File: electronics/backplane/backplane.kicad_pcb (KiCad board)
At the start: 2 copper layers, 46 x 100 mm, 22 parts, among them J1 USB_C_SOCKET_RA_PTH_SIMPLE, P1 JST_SH_4_RA, P2 JST_SH_4_RA, P3 JST_SH_4_RA, P4 JST_SH_4_RA, P5 PAD_SOLDER_2mm, SW1 B3U-1000P_SPST-NO_SMD, SW2 B3U-1000P_SPST-NO_SMD, U1 USBLC6, X1 MICROMOD_PROCESSOR_SOCKET, X2 SWD_SMT_SOCKET, X3 MICROMOD_FUNCTION_BOARD_SOCKET

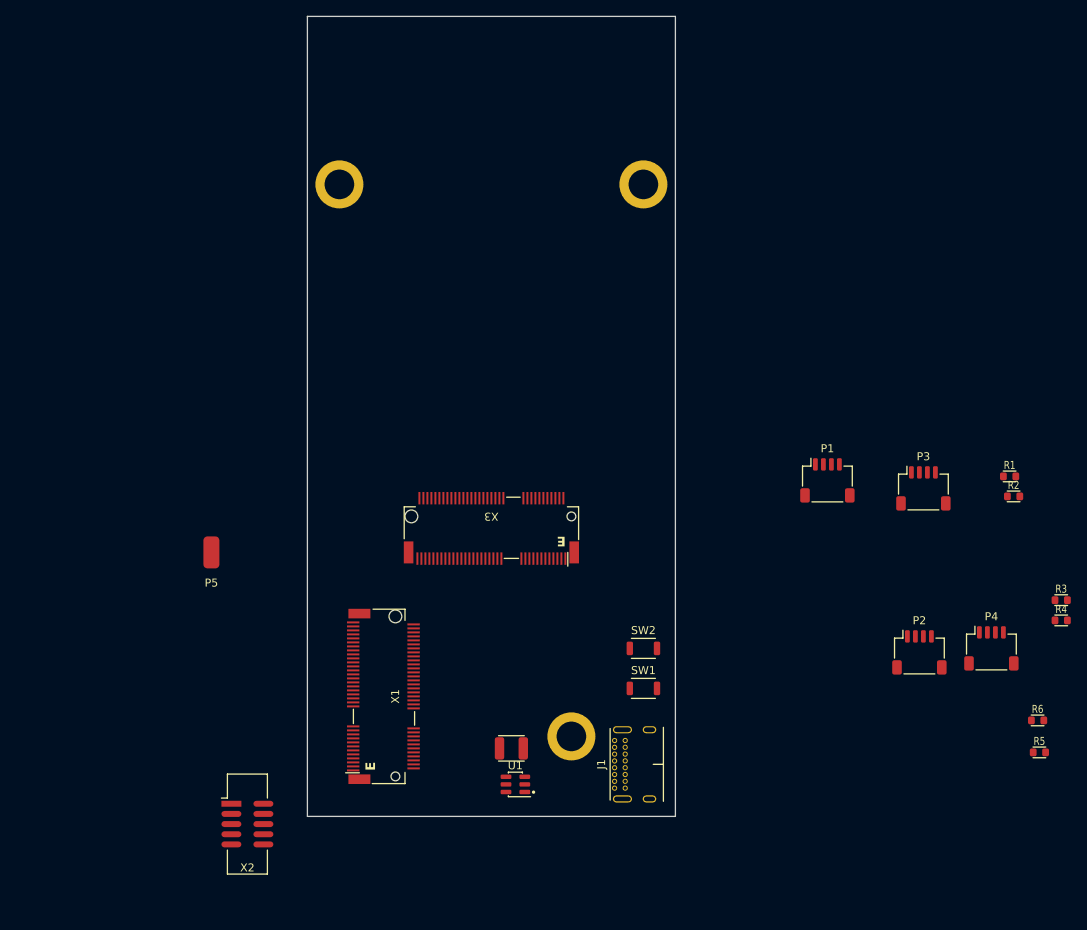
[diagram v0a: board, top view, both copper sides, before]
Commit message: Backplane schematic capture and PCB shape
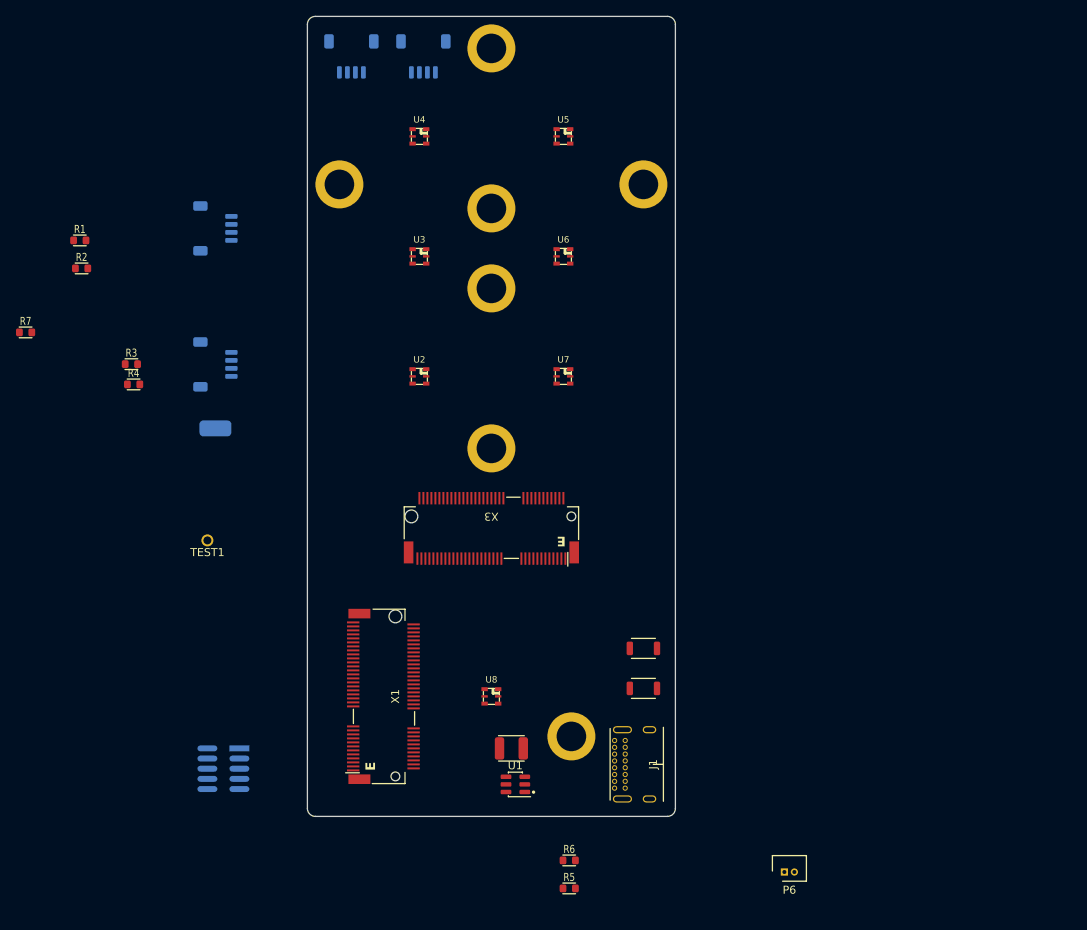
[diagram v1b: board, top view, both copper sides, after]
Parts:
- added MNT4: M2.5_SMD_4.0MM_THREADED, Applidyne_Mount:9774040151R, B.Cu at (123.0, 104.0)
- added MNT5: M2.5_SMD_4.0MM_THREADED, Applidyne_Mount:9774040151R, B.Cu at (123.0, 74.0)
- added MNT6: M2.5_SMD_4.0MM_THREADED, Applidyne_Mount:9774040151R, B.Cu at (123.0, 84.0)
- added MNT7: M2.5_SMD_4.0MM_THREADED, Applidyne_Mount:9774040151R, B.Cu at (123.0, 54.0)
- added P6: MOLEX_PICO_PTH_VERT_2_WAY, Applidyne_Connector_Molex:MOLEX_PICOBLADE_53047-0210, F.Cu at (159.6, 156.9)
- added R7: 10K0_1608M, Applidyne_Resistor:RESC1608X50N, F.Cu at (64.8, 89.5)
- added TEST1: CLIP_HOOK_PURPLE, Applidyne_Test:KEYSTONE_5119, F.Cu at (87.5, 115.5)
- added U2: APA102-2020, Applidyne_LED:AP102_200X200X90L, F.Cu at (114.0, 95.0)
- added U3: APA102-2020, Applidyne_LED:AP102_200X200X90L, F.Cu at (114.0, 80.0)
- added U4: APA102-2020, Applidyne_LED:AP102_200X200X90L, F.Cu at (114.0, 65.0)
- added U5: APA102-2020, Applidyne_LED:AP102_200X200X90L, F.Cu at (132.0, 65.0)
- added U6: APA102-2020, Applidyne_LED:AP102_200X200X90L, F.Cu at (132.0, 80.0)
- added U7: APA102-2020, Applidyne_LED:AP102_200X200X90L, F.Cu at (132.0, 95.0)
- added U8: APA102-2020, Applidyne_LED:AP102_200X200X90L, F.Cu at (123.0, 135.0)
- P1: value JST_SH_4_RA -> PAD_SOLDER_2mm; footprint Applidyne_Connector_JST:SM04B-SRSS-TB -> Applidyne_Connector:PAD_SOLDER_2mm; moved to B.Cu
- P2, P3, P4, X2: moved to B.Cu
- P5: value PAD_SOLDER_2mm -> JST_SH_4_RA; footprint Applidyne_Connector:PAD_SOLDER_2mm -> Applidyne_Connector_JST:SM04B-SRSS-TB; moved to B.Cu
- moved R2 119.9 mm to (71.8, 81.5)
- moved R1 119.9 mm to (71.5, 78.0)
- moved R3 119.9 mm to (78.0, 93.5)
- moved R4 119.6 mm to (78.3, 96.0)
- moved P4 103.3 mm to (88.5, 93.5), turned to 90 degrees
- moved P2 102.9 mm to (105.5, 55.0)
- moved P3 82.6 mm to (114.5, 55.0)
- moved P1 76.8 mm to (88.5, 101.5), turned to -90 degrees
- moved R5 61.2 mm to (132.7, 159.0)
- moved R6 61.1 mm to (132.7, 155.5)
- moved P5 40.5 mm to (88.5, 76.5), turned to 90 degrees
- moved X2 7.54 mm to (89.5, 144.0)
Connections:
- net /SWDCLK renamed /Processor/SWDCLK
- net /SWDIO renamed /Processor/SWDIO
- net /SWO renamed /Processor/SWO
- net /USBC_N renamed /USB Input/USBC_N
- net /USBC_P renamed /USB Input/USBC_P
- net /USB_D+ renamed /Processor/NATIVE.D+
- net /USB_D- renamed /Processor/NATIVE.D-
- net /USB_VCC renamed /Processor/USB_VCC
- net /~{BOOT} renamed /Processor/~{BOOT}
- net /~{RESET} renamed /Processor/~{RESET}
- MNT2 pad 1: unconnected-(MNT2-Pad1) -> GND
- MNT3 pad 1: unconnected-(MNT3-Pad1) -> GND
- P1 pad 1: GND -> /Expansion IO/~{I2C_INT}
- P2 pad 3: /I2C_SDA1 -> /Expansion IO/I2C_SDA0
- P2 pad 4: /I2C_SCL1 -> /Expansion IO/I2C_SCL0
- P3 pad 3: /I2C_SDA0 -> /Expansion IO/I2C_SDA1
- P3 pad 4: /I2C_SCL0 -> /Expansion IO/I2C_SCL1
- P4 pad 3: /I2C_SDA1 -> /Expansion IO/I2C_SDA0
- P4 pad 4: /I2C_SCL1 -> /Expansion IO/I2C_SCL0
- P5 pad 1: /~{I2C_INT} -> GND
- R1 pad 2: /I2C_SDA0 -> /Function Board/SDA
- R2 pad 2: /I2C_SCL0 -> /Function Board/SCL
- R3 pad 2: /I2C_SDA1 -> /Processor/I2C1.SDA
- R4 pad 2: /I2C_SCL1 -> /Processor/I2C1.SCL
- R5 pad 1: Net-(J1-CC2) -> Net-(J1-CC1)
- R6 pad 1: Net-(J1-CC1) -> Net-(J1-CC2)
- X1 pad 10: unconnected-(X1-D0-Pad10) -> /Function Board/FN_~{INT}
- X1 pad 12: /I2C_SDA0 -> /Function Board/SDA
- X1 pad 13: unconnected-(X1-UART_RTS1-Pad13) -> /Function Board/RTS
- X1 pad 14: /I2C_SCL0 -> /Function Board/SCL
- X1 pad 15: unconnected-(X1-UARTCTS1-Pad15) -> /Function Board/CTS
- X1 pad 16: /~{I2C_INT} -> /Function Board/~{FN_I2C_INT}
- X1 pad 17: unconnected-(X1-UART_TX1-Pad17) -> /Function Board/TX
- X1 pad 19: unconnected-(X1-UART_RX1-Pad19) -> /Function Board/RX
- X1 pad 2: unconnected-(X1-3V3-Pad2) -> +3.3V
- X1 pad 20: unconnected-(X1-UART_RX2-Pad20) -> /Processor/UART1.RX
- X1 pad 22: unconnected-(X1-UART_TX2-Pad22) -> /Processor/UART1.TX
- X1 pad 32: unconnected-(X1-PWM0-Pad32) -> /Function Board/FN_PWM
- X1 pad 34: unconnected-(X1-A0-Pad34) -> /Function Board/FN_ANALOG
- X1 pad 35: unconnected-(X1-USBHOST_D+-Pad35) -> /Function Board/D+
- X1 pad 37: unconnected-(X1-USBHOST_D--Pad37) -> /Function Board/D-
- X1 pad 4: unconnected-(X1-3V3_EN-Pad4) -> /Processor/3V3_PWR_EN
- X1 pad 40: unconnected-(X1-G0/BUS0-Pad40) -> /Function Board/G0
- X1 pad 41: unconnected-(X1-CAN_RX-Pad41) -> /Function Board/CAN.RX
- X1 pad 42: unconnected-(X1-G1/BUS1-Pad42) -> /Function Board/G1
- X1 pad 43: unconnected-(X1-CAN_TX-Pad43) -> /Function Board/CAN.TX
- X1 pad 44: unconnected-(X1-G2/BUS2-Pad44) -> /Function Board/G2
- X1 pad 46: unconnected-(X1-G3/BUS3-Pad46) -> /Function Board/G3
- X1 pad 48: unconnected-(X1-G4/BUS4-Pad48) -> /Function Board/G4
- X1 pad 51: /I2C_SDA1 -> /Processor/I2C1.SDA
- X1 pad 53: /I2C_SCL1 -> /Processor/I2C1.SCL
- X1 pad 55: unconnected-(X1-~{SPI_CS}-Pad55) -> /Function Board/~{CS}
- X1 pad 57: unconnected-(X1-SPI_SCK-Pad57) -> /Function Board/CLK
- X1 pad 59: unconnected-(X1-SPI_COPI-Pad59) -> /Function Board/COPI
- X1 pad 60: unconnected-(X1-SPI_SCK1/SDIO_CLK-Pad60) -> /Processor/SPI1.CLK
- X1 pad 61: unconnected-(X1-SPI_CIPO-Pad61) -> /Function Board/CIPO
- X1 pad 62: unconnected-(X1-SPI_COPI1/SDIO_CMD-Pad62) -> /Processor/SPI1.COPI
- X1 pad 64: unconnected-(X1-SPI_CIPO1/SDIO_DATA0-Pad64) -> /Processor/SPI1.CIPO
- X1 pad 70: unconnected-(X1-~{SPI_CS1}/SDIO_DATA3-Pad70) -> /Processor/SPI1.~{CS}
- X1 pad 74: unconnected-(X1-3V3-Pad74) -> +3.3V
- X3 pad 1: unconnected-(X3-GND-Pad1) -> GND
- X3 pad 13: unconnected-(X3-FUNC_TX-Pad13) -> /Function Board/RX
- X3 pad 15: unconnected-(X3-FUNC_RX-Pad15) -> /Function Board/TX
- X3 pad 16: unconnected-(X3-FUNC_RTS-Pad16) -> /Function Board/CTS
- X3 pad 18: unconnected-(X3-FUNC_CTS-Pad18) -> /Function Board/RTS
- X3 pad 19: unconnected-(X3-I2C_SDA-Pad19) -> /Function Board/SDA
- X3 pad 2: unconnected-(X3-GND-Pad2) -> GND
- X3 pad 21: unconnected-(X3-I2C_SCL-Pad21) -> /Function Board/SCL
- X3 pad 23: unconnected-(X3-~{I2C_INT}-Pad23) -> /Function Board/~{FN_I2C_INT}
- X3 pad 3: unconnected-(X3-SPI_SCK-Pad3) -> /Function Board/CLK
- X3 pad 32: unconnected-(X3-EEPROM_A2-Pad32) -> GND
- X3 pad 33: unconnected-(X3-GND-Pad33) -> GND
- X3 pad 34: unconnected-(X3-EEPROM_A1-Pad34) -> GND
- X3 pad 35: unconnected-(X3-USBHOST_D+-Pad35) -> /Function Board/D+
- X3 pad 36: unconnected-(X3-EEPROM_A0-Pad36) -> GND
- X3 pad 37: unconnected-(X3-USBHOST_D--Pad37) -> /Function Board/D-
- X3 pad 38: unconnected-(X3-A0-Pad38) -> /Function Board/FN_ANALOG
- X3 pad 39: unconnected-(X3-GND-Pad39) -> GND
- X3 pad 40: unconnected-(X3-EEPROM_WP-Pad40) -> Net-(TEST1-PAD)
- X3 pad 41: unconnected-(X3-CAN_TX-Pad41) -> /Function Board/CAN.RX
- X3 pad 43: unconnected-(X3-CAN_RX-Pad43) -> /Function Board/CAN.TX
- X3 pad 45: unconnected-(X3-GND-Pad45) -> GND
- X3 pad 47: unconnected-(X3-F0/~{INT}-Pad47) -> /Function Board/FN_~{INT}
- X3 pad 49: unconnected-(X3-F1/~{CS}-Pad49) -> /Function Board/~{CS}
- X3 pad 5: unconnected-(X3-SPI_SDI-Pad5) -> /Function Board/COPI
- X3 pad 51: unconnected-(X3-F2/PWM-Pad51) -> /Function Board/FN_PWM
- X3 pad 53: unconnected-(X3-F3-Pad53) -> /Function Board/G0
- X3 pad 55: unconnected-(X3-F4-Pad55) -> /Function Board/G1
- X3 pad 57: unconnected-(X3-F5-Pad57) -> /Function Board/G2
- X3 pad 59: unconnected-(X3-F6-Pad59) -> /Function Board/G3
- X3 pad 61: unconnected-(X3-F7-Pad61) -> /Function Board/G4
- X3 pad 7: unconnected-(X3-SPI_SDO-Pad7) -> /Function Board/CIPO
- X3 pad 71: unconnected-(X3-PWR_EN-Pad71) -> /Function Board/FN_PWR_EN
- X3 pad 72: unconnected-(X3-VCC-Pad72) -> Net-(X3-VCC-Pad72)
- X3 pad 73: unconnected-(X3-3V3-Pad73) -> +3.3V
- X3 pad 74: unconnected-(X3-VCC-Pad74) -> Net-(X3-VCC-Pad72)
- X3 pad 75: unconnected-(X3-GND-Pad75) -> GND
- X3 pad 8: unconnected-(X3-GND-Pad8) -> GND
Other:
- outline, holes or cut-outs redrawn
- copper layers 2 -> 4
- board text added: "QWIIC MODULE BAY"

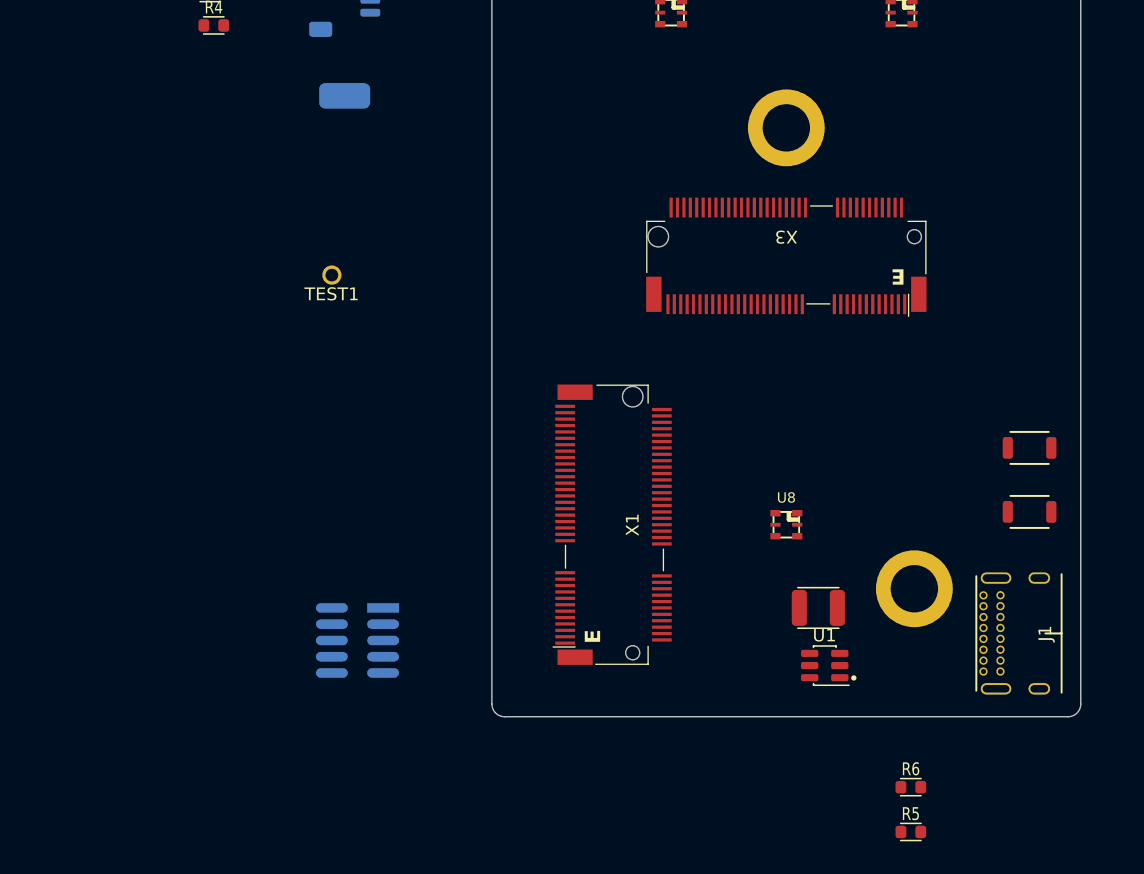
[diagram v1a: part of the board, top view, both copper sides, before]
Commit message: Continue backplane PCB
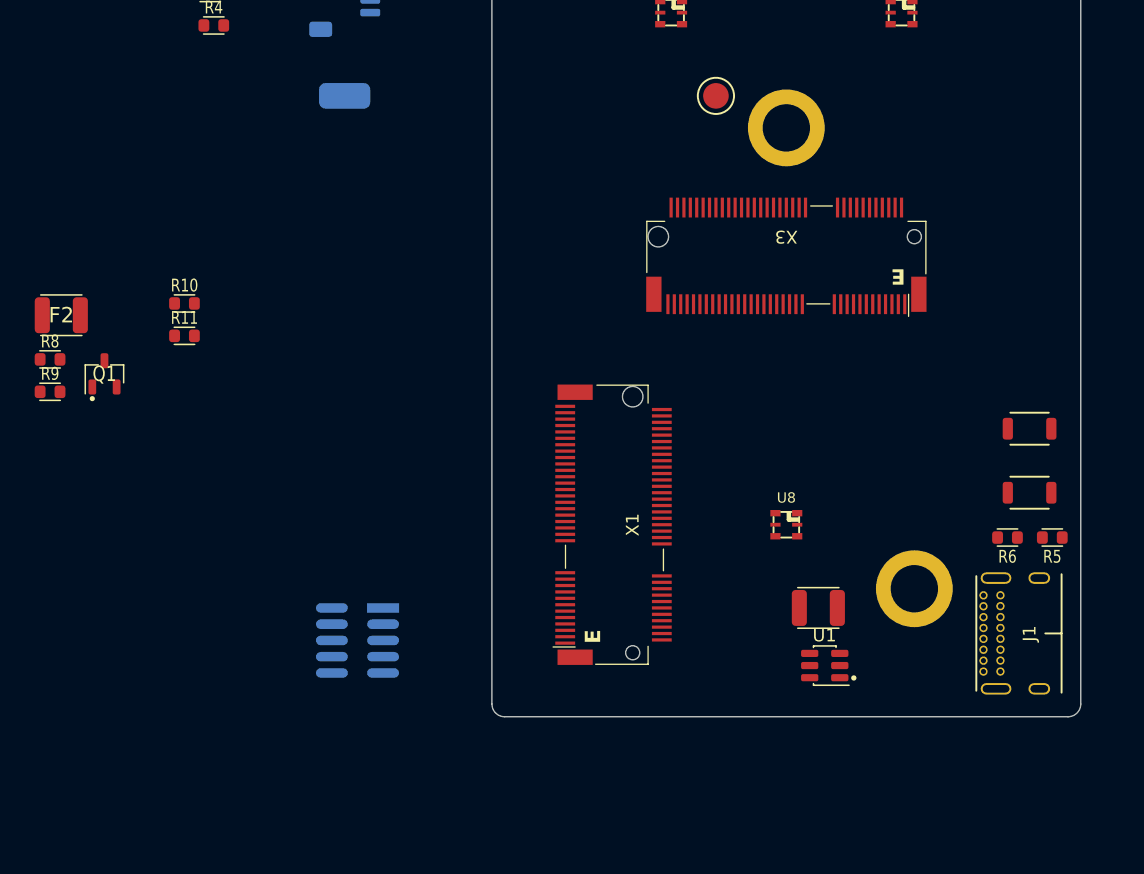
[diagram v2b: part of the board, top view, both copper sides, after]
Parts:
- removed TEST1: CLIP_HOOK_PURPLE, Applidyne_Test:KEYSTONE_5119
- added F2: 0.5A_1210L_PTC, Applidyne_Fuse:FUSC3225X85L50N, F.Cu at (66.4, 118.6)
- added Q1: 2N7002P, Applidyne_SOT:SOT95P240X110-3L16N, F.Cu at (69.7, 123.2)
- added R10: 20K0_1608M, Applidyne_Resistor:RESC1608X50N, F.Cu at (76.0, 117.7)
- added R11: 10K0_1608M, Applidyne_Resistor:RESC1608X50N, F.Cu at (76.0, 120.2)
- added R8: 10R_1608M, Applidyne_Resistor:RESC1608X50N, F.Cu at (65.5, 122.1)
- added R9: 10K0_1608M, Applidyne_Resistor:RESC1608X50N, F.Cu at (65.5, 124.6)
- added TEST2: PROBE_PAD, Applidyne_Test:TP200, F.Cu at (117.5, 101.5)
- moved R5 25.5 mm to (143.8, 136.0), turned to 180 degrees
- moved R6 20.9 mm to (140.3, 136.0)
- moved SW1 1.50 mm to (142.0, 132.5)
- moved SW2 1.50 mm to (142.0, 127.5)
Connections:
- net Net-(X3-VCC-Pad72) renamed +POWER
- P2 pad 3: /Expansion IO/I2C_SDA0 -> /Expansion IO/I2C0.SDA
- P2 pad 4: /Expansion IO/I2C_SCL0 -> /Expansion IO/I2C0.SCL
- P3 pad 3: /Expansion IO/I2C_SDA1 -> /Expansion IO/I2C1.SDA
- P3 pad 4: /Expansion IO/I2C_SCL1 -> /Expansion IO/I2C1.SCL
- P4 pad 3: /Expansion IO/I2C_SDA0 -> /Expansion IO/I2C0.SDA
- P4 pad 4: /Expansion IO/I2C_SCL0 -> /Expansion IO/I2C0.SCL
- P5 pad 3: /Expansion IO/I2C_SDA1 -> /Expansion IO/I2C1.SDA
- P5 pad 4: /Expansion IO/I2C_SCL1 -> /Expansion IO/I2C1.SCL
- R1 pad 2: /Function Board/SDA -> /Expansion IO/I2C0.SDA
- R2 pad 2: /Function Board/SCL -> /Expansion IO/I2C0.SCL
- R3 pad 2: /Processor/I2C1.SDA -> /Expansion IO/I2C1.SDA
- R4 pad 2: /Processor/I2C1.SCL -> /Expansion IO/I2C1.SCL
- R7 pad 2: /Function Board/~{FN_I2C_INT} -> /Expansion IO/~{I2C_INT}
- X1 pad 12: /Function Board/SDA -> /Expansion IO/I2C0.SDA
- X1 pad 14: /Function Board/SCL -> /Expansion IO/I2C0.SCL
- X1 pad 16: /Function Board/~{FN_I2C_INT} -> /Expansion IO/~{I2C_INT}
- X1 pad 18: unconnected-(X1-D1/CAM_TRIG-Pad18) -> /Processor/D1
- X1 pad 38: unconnected-(X1-A1-Pad38) -> /Processor/ADC1
- X1 pad 47: unconnected-(X1-PWM1-Pad47) -> /Processor/PWM1
- X1 pad 49: unconnected-(X1-BATT_VIN/3-Pad49) -> Net-(X1-BATT_VIN/3)
- X1 pad 51: /Processor/I2C1.SDA -> /Expansion IO/I2C1.SDA
- X1 pad 53: /Processor/I2C1.SCL -> /Expansion IO/I2C1.SCL
- X3 pad 19: /Function Board/SDA -> /Expansion IO/I2C0.SDA
- X3 pad 21: /Function Board/SCL -> /Expansion IO/I2C0.SCL
- X3 pad 23: /Function Board/~{FN_I2C_INT} -> /Expansion IO/~{I2C_INT}

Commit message: Continue backplane
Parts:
- removed P5: JST_SH_4_RA, Applidyne_Connector_JST:SM04B-SRSS-TB
- removed P6: MOLEX_PICO_PTH_VERT_2_WAY, Applidyne_Connector_Molex:MOLEX_PICOBLADE_53047-0210
- removed U2, U3, U4, U5, U6, U7, U8: APA102-2020, Applidyne_LED:AP102_200X200X90L
- added C1: 10u_X7R_2012M, Applidyne_Capacitor:CAPC2012X110N, F.Cu at (162.1, 113.3)
- added C2: 10u_X7R_2012M, Applidyne_Capacitor:CAPC2012X110N, F.Cu at (162.1, 116.3)
- added C3: 10u_X7R_2012M, Applidyne_Capacitor:CAPC2012X110N, F.Cu at (162.1, 119.3)
- added R12: 10K0_1608M, Applidyne_Resistor:RESC1608X50N, F.Cu at (166.3, 118.2)
- added R13: 10R_1608M, Applidyne_Resistor:RESC1608X50N, F.Cu at (166.3, 120.8)
- added R14: 0R_QUAD_ARRAY_1608M, Applidyne_Resistor:R_Array_Concave_4x1608M, F.Cu at (152.7, 118.8)
- added SL1: SOLDER-LINK-2-TINY, Applidyne_Link:SJ1005-2N, F.Cu at (116.5, 125.5)
- added SL2: SOLDER-LINK-2-TINY, Applidyne_Link:SJ1005-2N, F.Cu at (96.5, 94.8)
- added SL3: SOLDER-LINK-2-TINY, Applidyne_Link:SJ1005-2N, F.Cu at (96.5, 96.5)
- added U9: AP2112K-3.3, Applidyne_SOT:SOT95P280X145-5L30N, F.Cu at (166.6, 114.4)
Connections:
- net /Processor/UART1.RX renamed /Expansion IO/RX
- net /Processor/UART1.TX renamed /Expansion IO/TX
- net /Processor/USB_VCC renamed /Power Regulation/USB_VCC
- X1 pad 4: /Processor/3V3_PWR_EN -> unconnected-(X1-3V3_EN-Pad4)
- X1 pad 65: unconnected-(X1-G9/ADC_D-/CAM_HSYNC-Pad65) -> /Processor/G9
- X1 pad 67: unconnected-(X1-G8-Pad67) -> /Processor/G8
- X1 pad 69: unconnected-(X1-G7/BUS7-Pad69) -> /Processor/G7
- X1 pad 71: unconnected-(X1-G6/BUS6-Pad71) -> /Processor/G6
- X1 pad 72: unconnected-(X1-RTC_3V_BATT-Pad72) -> Net-(X1-RTC_3V_BATT)
- X1 pad 73: unconnected-(X1-G5/BUS5-Pad73) -> /Processor/G5
- X3 pad 13: /Function Board/RX -> Net-(X3-FUNC_TX)
- X3 pad 15: /Function Board/TX -> Net-(X3-FUNC_RX)
- X3 pad 16: /Function Board/CTS -> Net-(X3-FUNC_RTS)
- X3 pad 18: /Function Board/RTS -> Net-(X3-FUNC_CTS)
